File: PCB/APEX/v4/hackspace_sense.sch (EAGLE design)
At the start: 9 parts

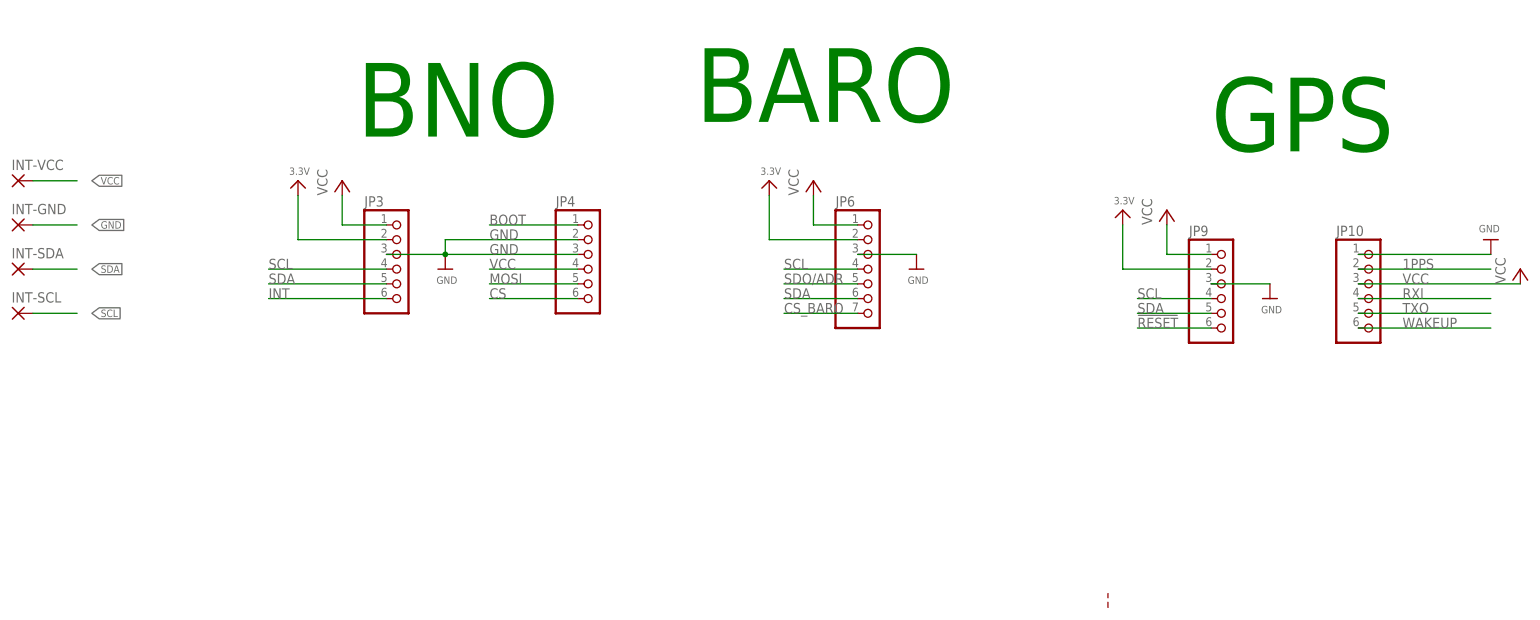
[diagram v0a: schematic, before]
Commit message: embiggen pads
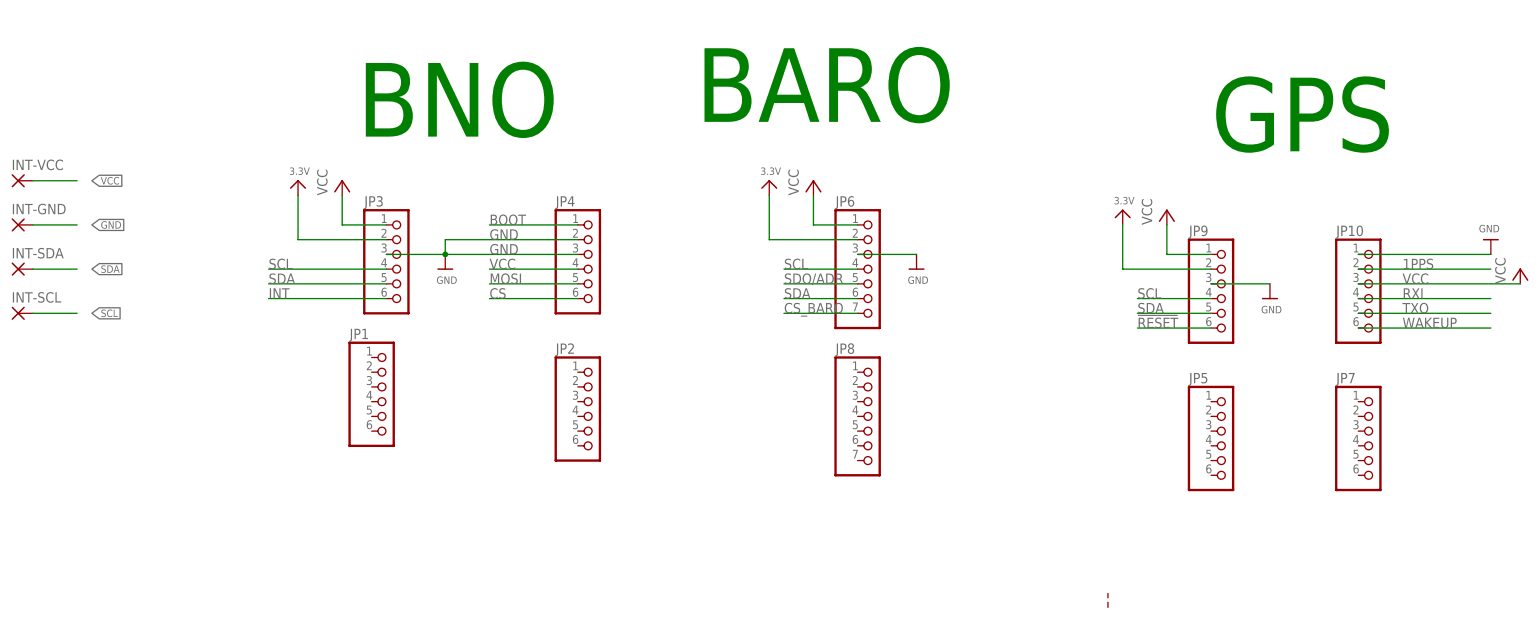
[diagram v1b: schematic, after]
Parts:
- added JP1, JP2, JP5, JP7: (no value), pinhead:PINHD-1X6
- added JP8: (no value), pinhead:PINHD-1X7
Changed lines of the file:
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@@
 <part name="U$13" library="microbuilder" deviceset="GND" device=""/>
 <part name="P+8" library="supply1" library_urn="urn:adsk.eagle:library:371" deviceset="VCC" device=""/>
+<part name="JP1" library="pinhead" library_urn="urn:adsk.eagle:library:325" deviceset="PINHD-1X6" device="" package3d_urn="urn:adsk.eagle:package:22472/2"/>
+<part name="JP2" library="pinhead" library_urn="urn:adsk.eagle:library:325" deviceset="PINHD-1X6" device="" package3d_urn="urn:adsk.eagle:package:22472/2"/>
+<part name="JP5" library="pinhead" library_urn="urn:adsk.eagle:library:325" deviceset="PINHD-1X6" device="" package3d_urn="urn:adsk.eagle:package:22472/2"/>
+<part name="JP7" library="pinhead" library_urn="urn:adsk.eagle:library:325" deviceset="PINHD-1X6" device="" package3d_urn="urn:adsk.eagle:package:22472/2"/>
+<part name="JP8" library="pinhead" library_urn="urn:adsk.eagle:library:325" deviceset="PINHD-1X7" device="" package3d_urn="urn:adsk.eagle:package:22477/2"/>
 </parts>
 <sheets>
@@
 <attribute name="VALUE" x="304.8" y="45.72" size="1.778" layer="96" rot="R90"/>
 </instance>
+<instance part="JP1" gate="A" x="111.76" y="25.4" smashed="yes">
+<attribute name="NAME" x="105.41" y="36.195" size="1.778" layer="95"/>
+<attribute name="VALUE" x="105.41" y="15.24" size="1.778" layer="96"/>
+</instance>
+<instance part="JP2" gate="A" x="147.32" y="22.86" smashed="yes">
+<attribute name="NAME" x="140.97" y="33.655" size="1.778" layer="95"/>
+<attribute name="VALUE" x="140.97" y="12.7" size="1.778" layer="96"/>
+</instance>
+<instance part="JP5" gate="A" x="256.54" y="17.78" smashed="yes">
+<attribute name="NAME" x="250.19" y="28.575" size="1.778" layer="95"/>
+<attribute name="VALUE" x="250.19" y="7.62" size="1.778" layer="96"/>
+</instance>
+<instance part="JP7" gate="A" x="281.94" y="17.78" smashed="yes">
+<attribute name="NAME" x="275.59" y="28.575" size="1.778" layer="95"/>
+<attribute name="VALUE" x="275.59" y="7.62" size="1.778" layer="96"/>
+</instance>
+<instance part="JP8" gate="A" x="195.58" y="22.86" smashed="yes">
+<attribute name="NAME" x="189.23" y="33.655" size="1.778" layer="95"/>
+<attribute name="VALUE" x="189.23" y="10.16" size="1.778" layer="96"/>
+</instance>
 </instances>
